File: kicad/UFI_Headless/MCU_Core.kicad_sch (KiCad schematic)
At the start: 67 parts, among them J12 FRONT_LED, J13 MODE_SW, J4 SWD, J5 DBG_UART, J9 EXPANSION, SW1 RESET, SW2 BOOT, SW3 BTN_A, SW4 BTN_B, U11 APS6404L-3SQR-SN, U15 CSNP32GCR01-AOW, U5 STM32H723ZGT6, Y1 25MHz CL=12pF

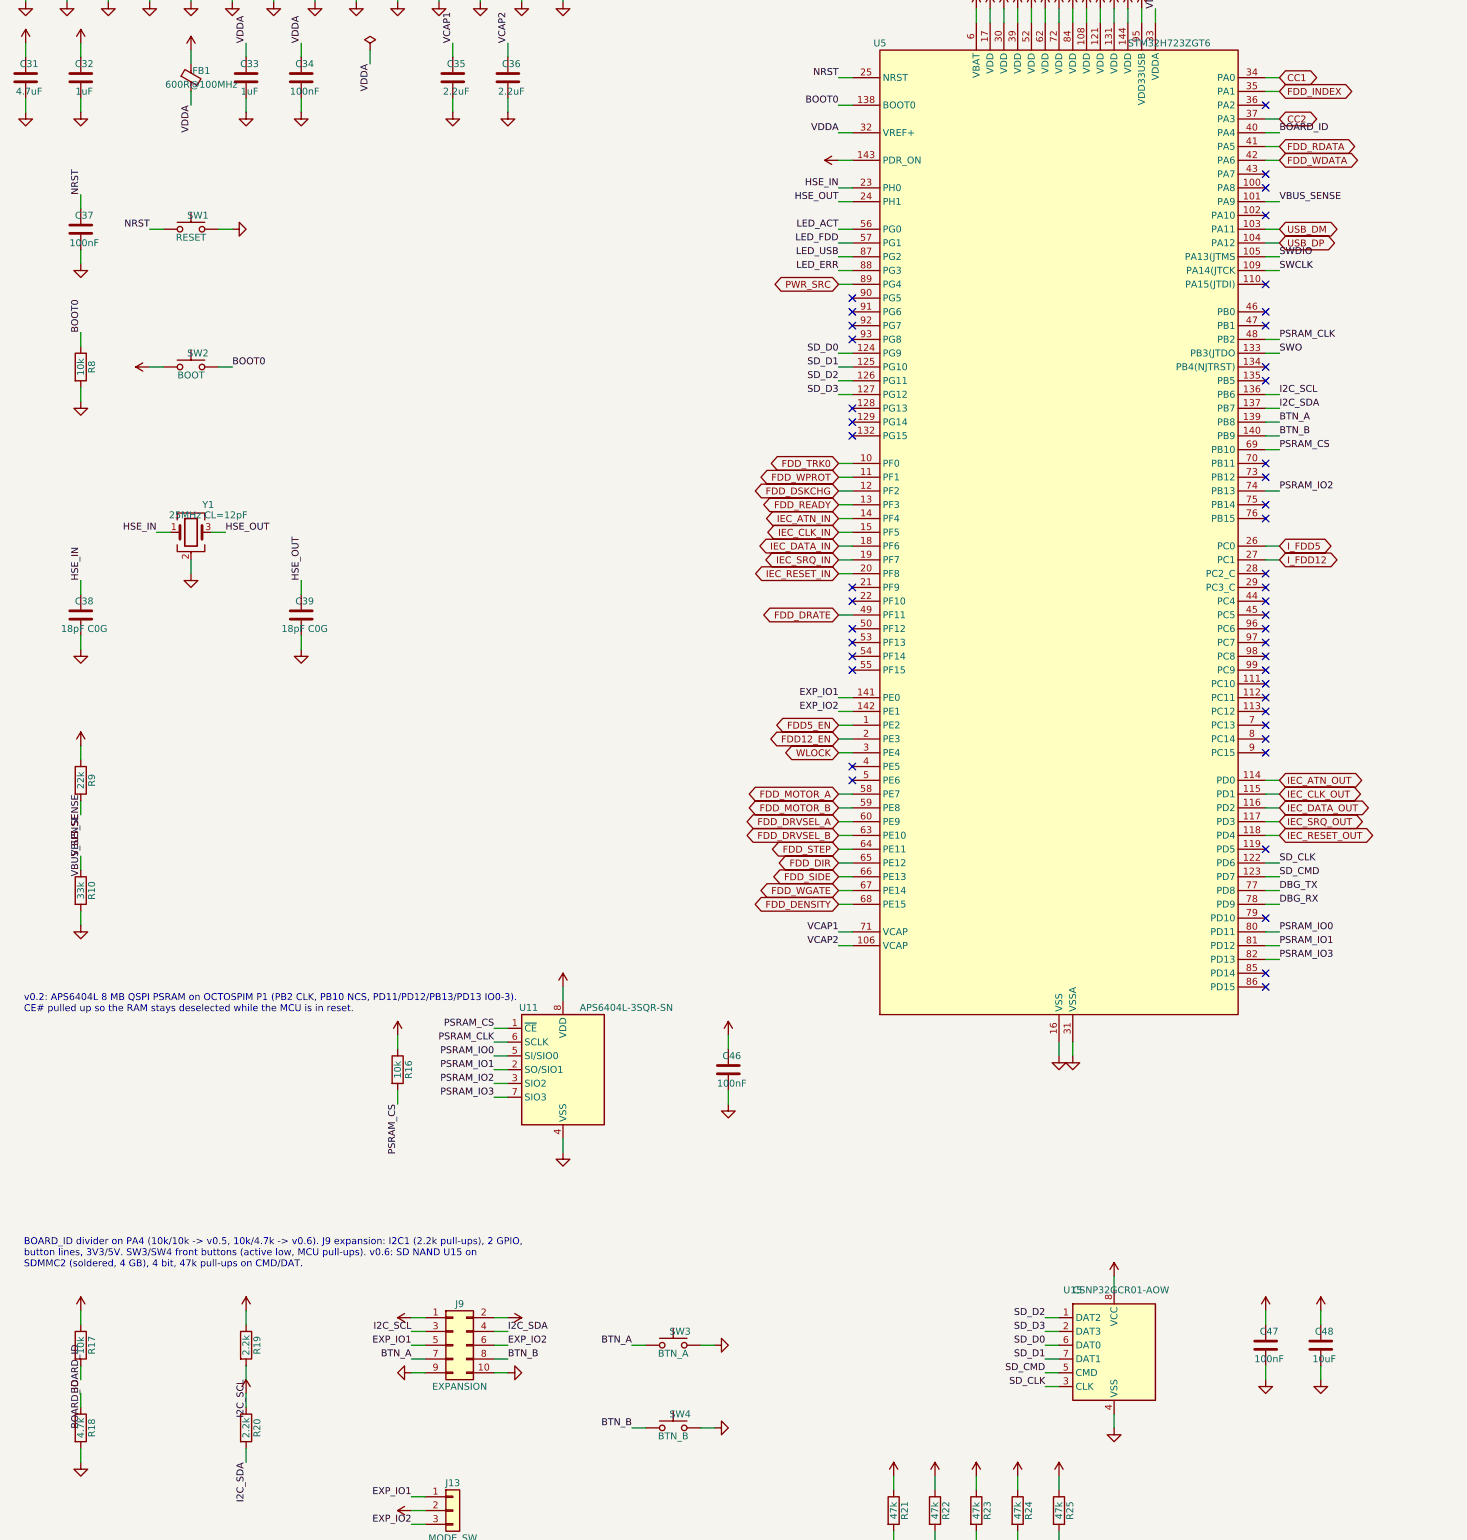
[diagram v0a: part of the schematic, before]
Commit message: v0.7: Apple Disk II port (J14/J15), board 110 x 97 mm; firmware 1.11: drives apple/apple2
Board
- Apple_Port sheet: J14 2x10 (Disk II controller pinout), SN74AHCT244 outputs at FDD_5V
  (phases, /ENABLE 1+2, /WRREQ, WRDATA), 74LVC2G17 inputs (RDDATA, WRPROT), ICL7662 -12V
  from FDD_12V, reset-safe 10k arrays, ESD on all port lines, J15 = /ENABLE drive 2
- MCU: RDDATA PA2 (TIM2_CH3), WRDATA PA7 (TIM3_CH2), PH0/1/3 PF12/13/15, PH2 PG6,
  EN1 PG5, EN2 PB12, WRREQ PB14, WRPROT PB15; board ID 10k/2.2k = v0.7
- outline +12 mm (eco/extend_outline.py), mounting holes H5/H6, ECO + Freerouting, hand
  routes for EN1/PH2 (PB11/PF14 unreachable), FDD_12V to J14/U18, D16 GND via;
  J14 uses a project copy of the IDC footprint (silk edge clears the J7 pin-1 mark)
- DRC 0 incl. warnings, unconnected 0, parity 0, via-in-pad 0; fab outputs regenerated

Firmware 1.11
- Disk II stepper (4 phases, half tracks, recalibrate = 80 half steps to the stop, phases
  off between seeks), /ENABLE = motor, write protect, no disk change / always ready
- capture input switch CH1/CH3 (DMAMUX), Apple reads in 200 ms slices (no index)
- writes: TIM3_CH2 toggle mode, /WRREQ, start without index, no precomp; erase = /WRREQ
- Apple drives selectable only on a v0.7 board (board ID); UFI.CFG drive=apple/apple2,
  SCP disk type Apple II without index flag; host drive name apple2
- dump simulation: SCP still byte-identical; host tests pass

Docs: README Apple section + GPIO table, bring-up 7.2f-7.2j, order list v0.7
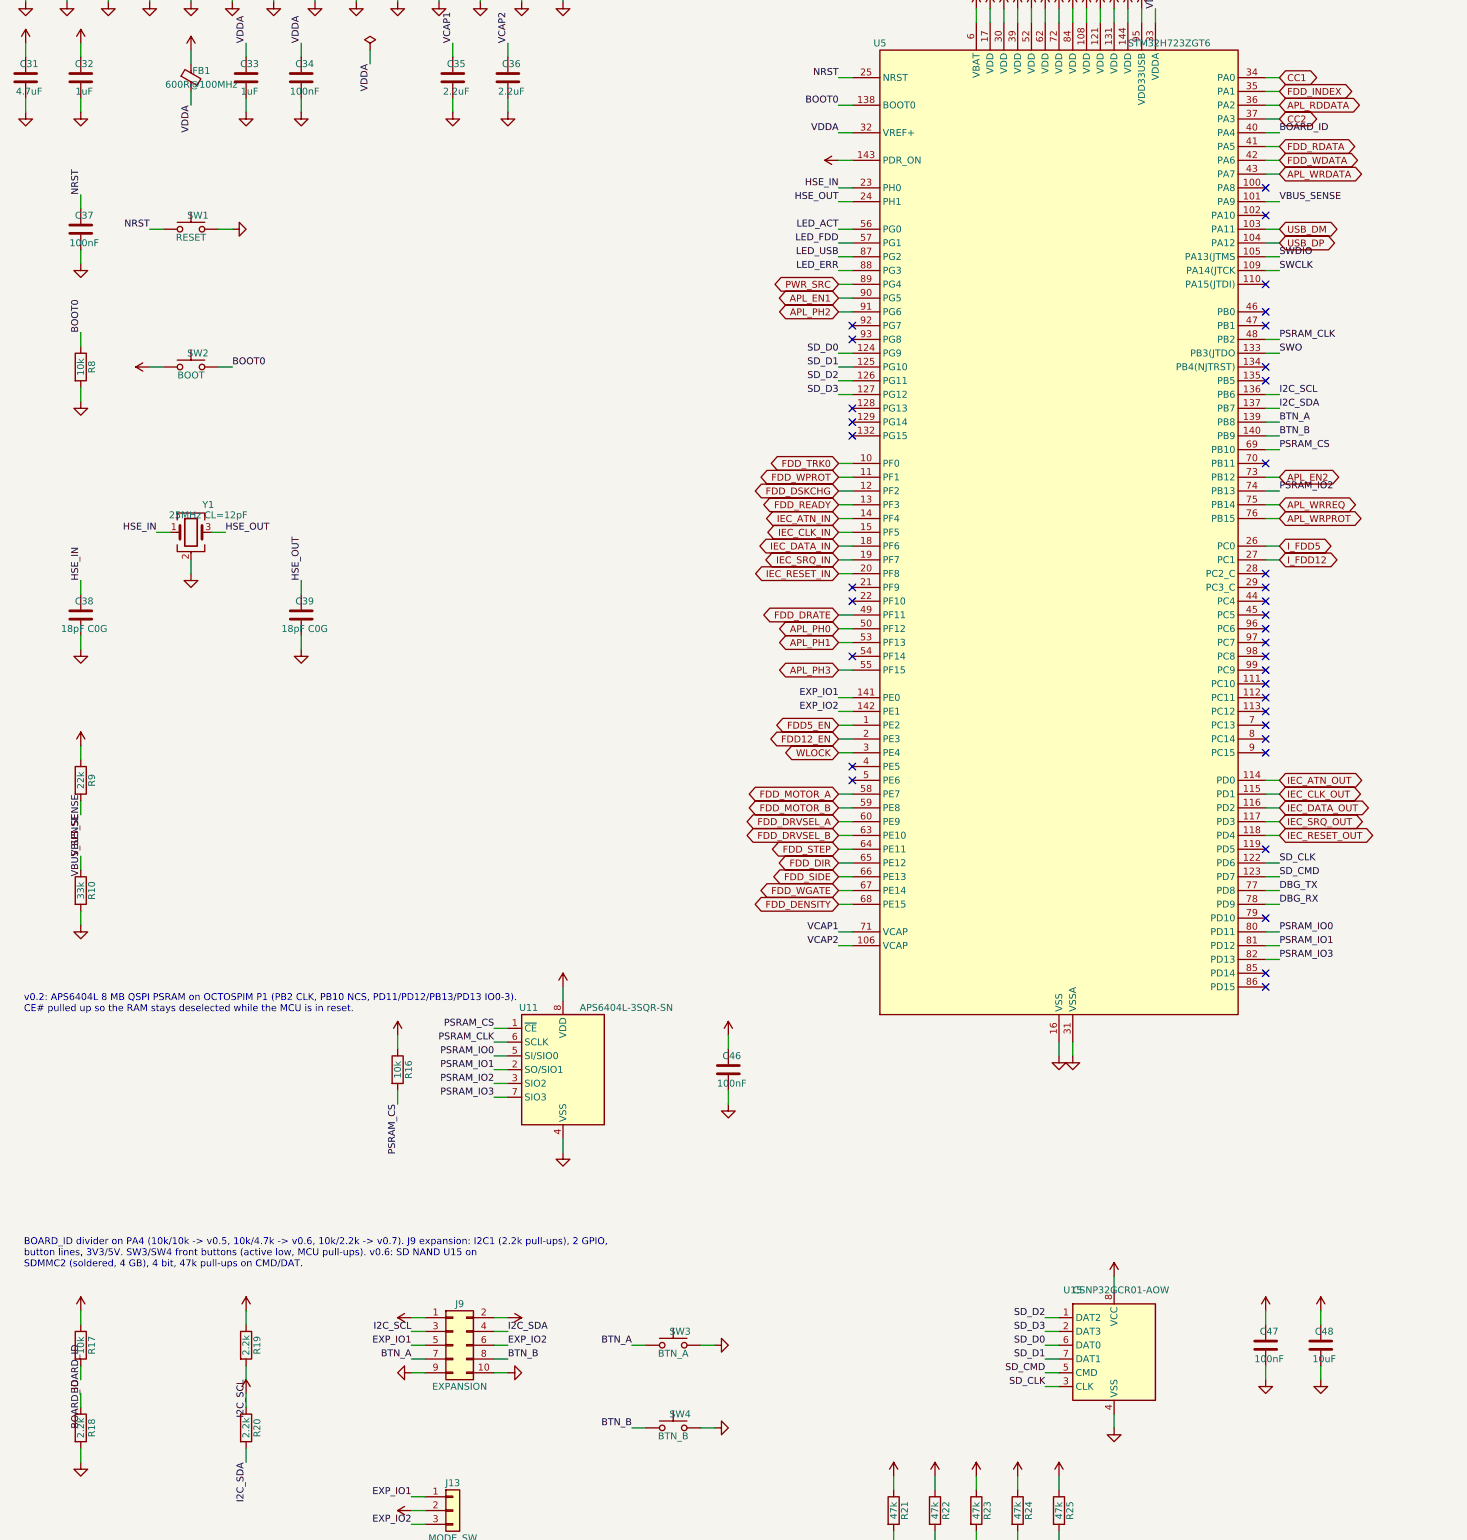
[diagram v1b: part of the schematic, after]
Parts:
- R18: value 4.7k -> 2.2k; LCSC C23162 -> C4190
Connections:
- net APL_RDDATA: now reaches U5.36 (PA2)
- net APL_WRDATA: now reaches U5.43 (PA7)
- net APL_PH0: now reaches U5.50 (PF12)
- net APL_PH1: now reaches U5.53 (PF13)
- net APL_PH3: now reaches U5.55 (PF15)
- net APL_EN2: now reaches U5.73 (PB12)
- net APL_WRREQ: now reaches U5.75 (PB14)
- net APL_WRPROT: now reaches U5.76 (PB15)
- net APL_EN1: now reaches U5.90 (PG5)
- net APL_PH2: now reaches U5.91 (PG6)
- no-connect marks 48 -> 38
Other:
- note added: "BOARD_ID divider on PA4 (10k/10k -> v0.5, 10k/4.7k -> v0.6, 10k/2.2k -> v0.7). J9 expansion: I2C1 (2.2k pull-ups), 2 GPIO, button lines, 3V3/5V. SW3/SW4 front buttons (active low, MCU pull-ups). v0.6: SD NAND U15 on SDMMC2 (soldered, 4 GB), 4 bit, 47k pull-ups on CMD/DAT."
- note removed: "BOARD_ID divider on PA4 (10k/10k -> v0.5, 10k/4.7k -> v0.6). J9 expansion: I2C1 (2.2k pull-ups), 2 GPIO, button lines, 3V3/5V. SW3/SW4 front buttons (active low, MCU pull-ups). v0.6: SD NAND U15 on SDMMC2 (soldered, 4 GB), 4 bit, 47k pull-ups on CMD/DAT."
